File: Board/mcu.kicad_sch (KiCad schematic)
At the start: 5 parts, among them J1 USB_C_Receptacle_USB2.0_14P, U1 NCP1117-3.3_SOT223, U2 RP2040

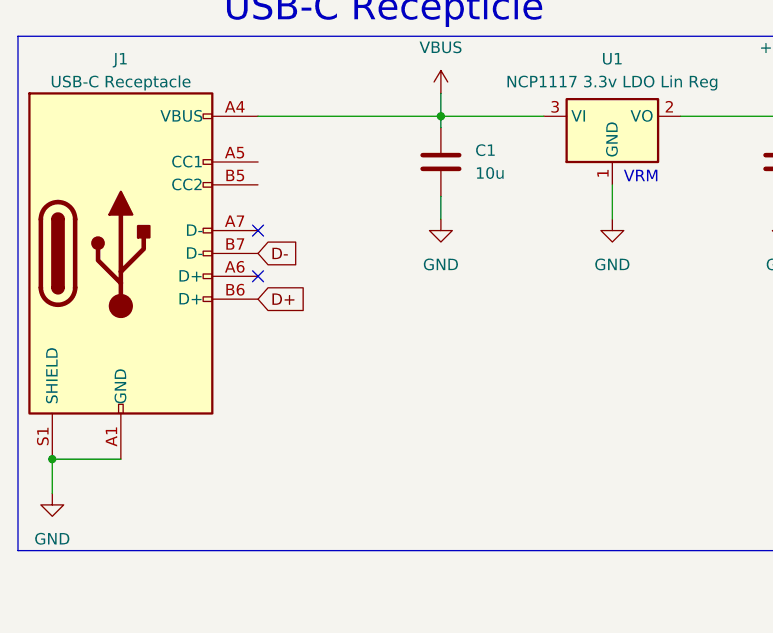
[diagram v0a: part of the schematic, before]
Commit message: Added pulldowns to USBC Receptacle CC1 and CC2 pins
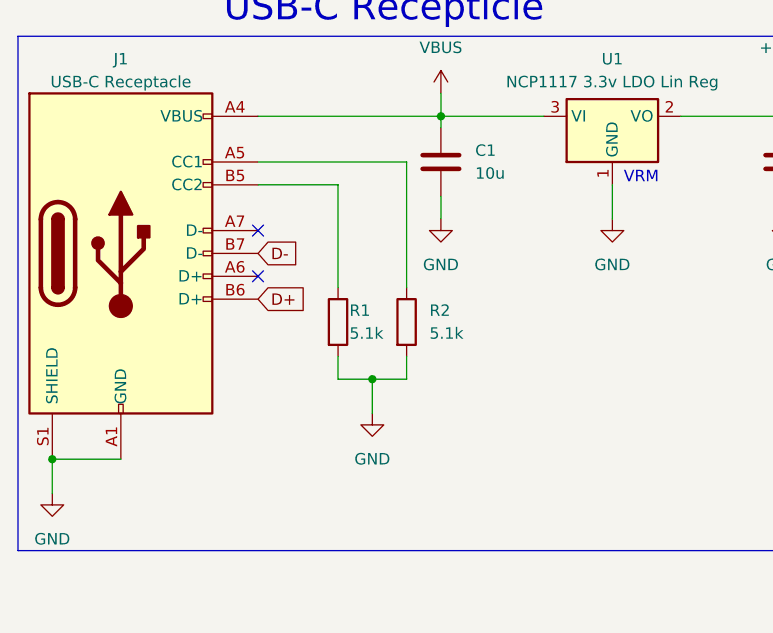
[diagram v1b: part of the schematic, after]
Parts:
- added R1, R2: 5.1k, Resistor_SMD:R_0603_1608Metric, symbol Device:R
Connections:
- net GND: now also R1.2, R2.2
- net at J1.A5 (CC1): now also R2.1
- net at J1.B5 (CC2): now also R1.1
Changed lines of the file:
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@@
   (junction (at 66.04 36.83) (diameter 0) (color 0 0 0 0)
+  )
+  (junction (at 58.42 66.04) (diameter 0) (color 0 0 0 0)
   )
   (junction (at 104.14 36.83) (diameter 0) (color 0 0 0 0)
@@
   (no_connect (at 45.72 49.53))
   (no_connect (at 45.72 54.61))
+  (wire (pts (xy 62.23 66.04) (xy 62.23 63.5))
+    (stroke (width 0) (type default))
+  )
+  (wire (pts (xy 58.42 66.04) (xy 62.23 66.04))
+    (stroke (width 0) (type default))
+  )
   (wire (pts (xy 66.04 48.26) (xy 66.04 45.72))
     (stroke (width 0) (type default))
   )
+  (wire (pts (xy 54.61 63.5) (xy 54.61 66.04))
+    (stroke (width 0) (type default))
+  )
   (wire (pts (xy 22.86 74.93) (xy 30.48 74.93))
     (stroke (width 0) (type default))
@@
     (stroke (width 0) (type default))
   )
+  (wire (pts (xy 45.72 41.91) (xy 62.23 41.91))
+    (stroke (width 0) (type default))
+  )
   (wire (pts (xy 45.72 36.83) (xy 66.04 36.83))
     (stroke (width 0) (type default))
   )
+  (wire (pts (xy 54.61 44.45) (xy 54.61 55.88))
+    (stroke (width 0) (type default))
+  )
   (wire (pts (xy 22.86 74.93) (xy 22.86 78.74))
     (stroke (width 0) (type default))
   )
+  (wire (pts (xy 58.42 66.04) (xy 58.42 69.85))
+    (stroke (width 0) (type default))
+  )
   (wire (pts (xy 104.14 34.29) (xy 104.14 36.83))
     (stroke (width 0) (type default))
@@
     (stroke (width 0) (type default))
   )
+  (wire (pts (xy 62.23 41.91) (xy 62.23 55.88))
+    (stroke (width 0) (type default))
+  )
+  (wire (pts (xy 45.72 44.45) (xy 54.61 44.45))
+    (stroke (width 0) (type default))
+  )
   (wire (pts (xy 104.14 36.83) (xy 104.14 38.1))
+    (stroke (width 0) (type default))
+  )
+  (wire (pts (xy 54.61 66.04) (xy 58.42 66.04))
     (stroke (width 0) (type default))
   )
@@
     (property "Intersheetrefs" "${INTERSHEET_REFS}" (at 51.5476 52.07 0)
       (effects (font (size 1.27 1.27)) (justify left) hide)
+    )
+  )
+  (symbol (lib_id "power:GND") (at 58.42 69.85 0) (unit 1)
+    (in_bom yes) (on_board yes) (dnp no) (fields_autoplaced)
+    (property "Reference" "#PWR07" (at 58.42 76.2 0)
+      (effects (font (size 1.27 1.27)) hide)
+    )
+    (property "Value" "GND" (at 58.42 74.93 0)
+      (effects (font (size 1.27 1.27)))
+    )
+    (property "Footprint" "" (at 58.42 69.85 0)
+      (effects (font (size 1.27 1.27)) hide)
+    )
+    (property "Datasheet" "" (at 58.42 69.85 0)
+      (effects (font (size 1.27 1.27)) hide)
+    )
+    (pin "1")
+    (instances
+      (project "ND68"
+        (path "/f6515d16-f8c0-46c5-adb6-b60d73ae282b/e7d003c3-21c2-4dac-954e-30d7425e12ae"
+          (reference "#PWR07") (unit 1)
+        )
+      )
+    )
+  )
+  (symbol (lib_id "Device:R") (at 54.61 59.69 0) (unit 1)
+    (in_bom yes) (on_board yes) (dnp no)
+    (property "Reference" "R1" (at 55.88 58.42 0)
+      (effects (font (size 1.27 1.27)) (justify left))
+    )
+    (property "Value" "5.1k" (at 55.88 60.96 0)
+      (effects (font (size 1.27 1.27)) (justify left))
+    )
+    (property "Footprint" "Resistor_SMD:R_0603_1608Metric" (at 52.832 59.69 90)
+      (effects (font (size 1.27 1.27)) hide)
+    )
+    (property "Datasheet" "~" (at 54.61 59.69 0)
+      (effects (font (size 1.27 1.27)) hide)
+    )
+    (property "DigiKey" "311-5.10KHRCT-ND" (at 54.61 59.69 0)
+      (effects (font (size 1.27 1.27)) hide)
+    )
+    (pin "2")
+    (pin "1")
+    (instances
+      (project "ND68"
+        (path "/f6515d16-f8c0-46c5-adb6-b60d73ae282b/e7d003c3-21c2-4dac-954e-30d7425e12ae"
+          (reference "R1") (unit 1)
+        )
+      )
     )
   )
@@
         )
       )
+    )
+  )
+  (symbol (lib_id "Device:R") (at 62.23 59.69 0) (unit 1)
+    (in_bom yes) (on_board yes) (dnp no) (fields_autoplaced)
+    (property "Reference" "R2" (at 64.77 58.42 0)
+      (effects (font (size 1.27 1.27)) (justify left))
+    )
+    (property "Value" "5.1k" (at 64.77 60.96 0)
+      (effects (font (size 1.27 1.27)) (justify left))
+    )
+    (property "Footprint" "Resistor_SMD:R_0603_1608Metric" (at 60.452 59.69 90)
+      (effects (font (size 1.27 1.27)) hide)
+    )
+    (property "Datasheet" "~" (at 62.23 59.69 0)
+      (effects (font (size 1.27 1.27)) hide)
+    )
+    (property "DigiKey" "311-5.10KHRCT-ND" (at 62.23 59.69 0)
+      (effects (font (size 1.27 1.27)) hide)
+    )
+    (pin "2")
+    (pin "1")
+    (instances
+      (project "ND68"
+        (path "/f6515d16-f8c0-46c5-adb6-b60d73ae282b/e7d003c3-21c2-4dac-954e-30d7425e12ae"
+          (reference "R2") (unit 1)
+        )
+      )

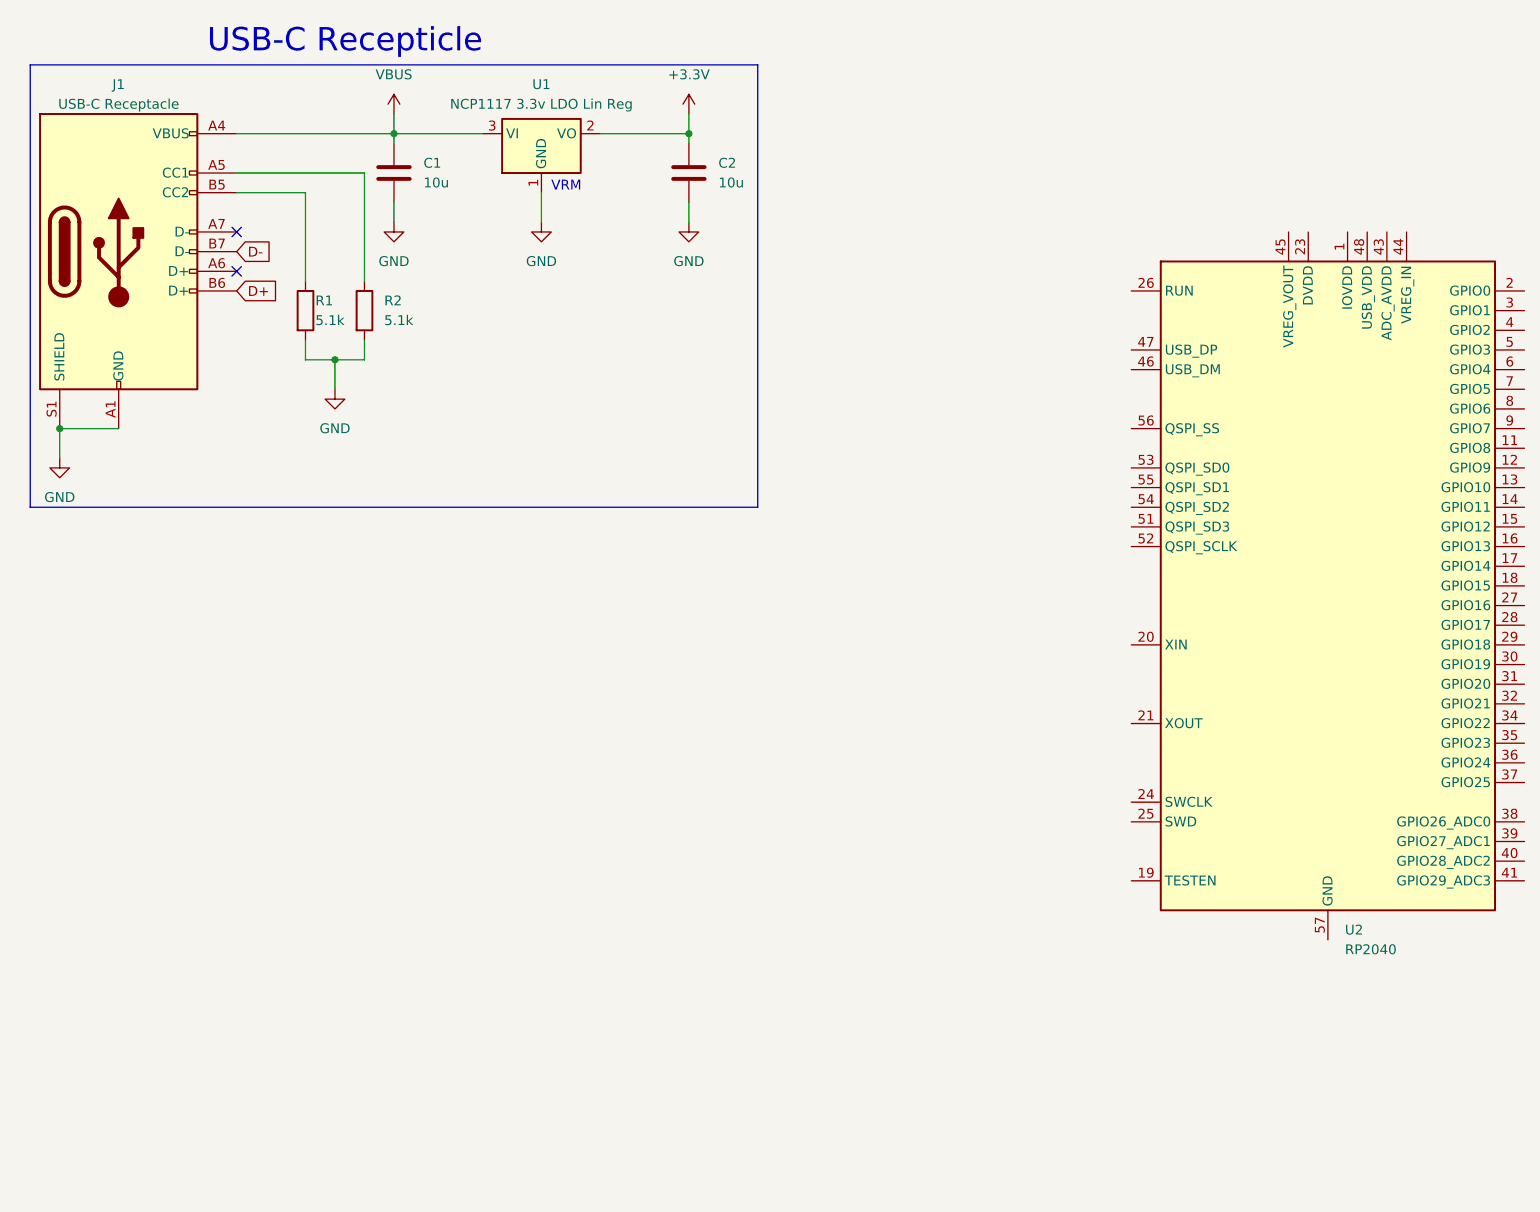
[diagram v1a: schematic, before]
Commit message: Added mcu power pin decoupling capacitors
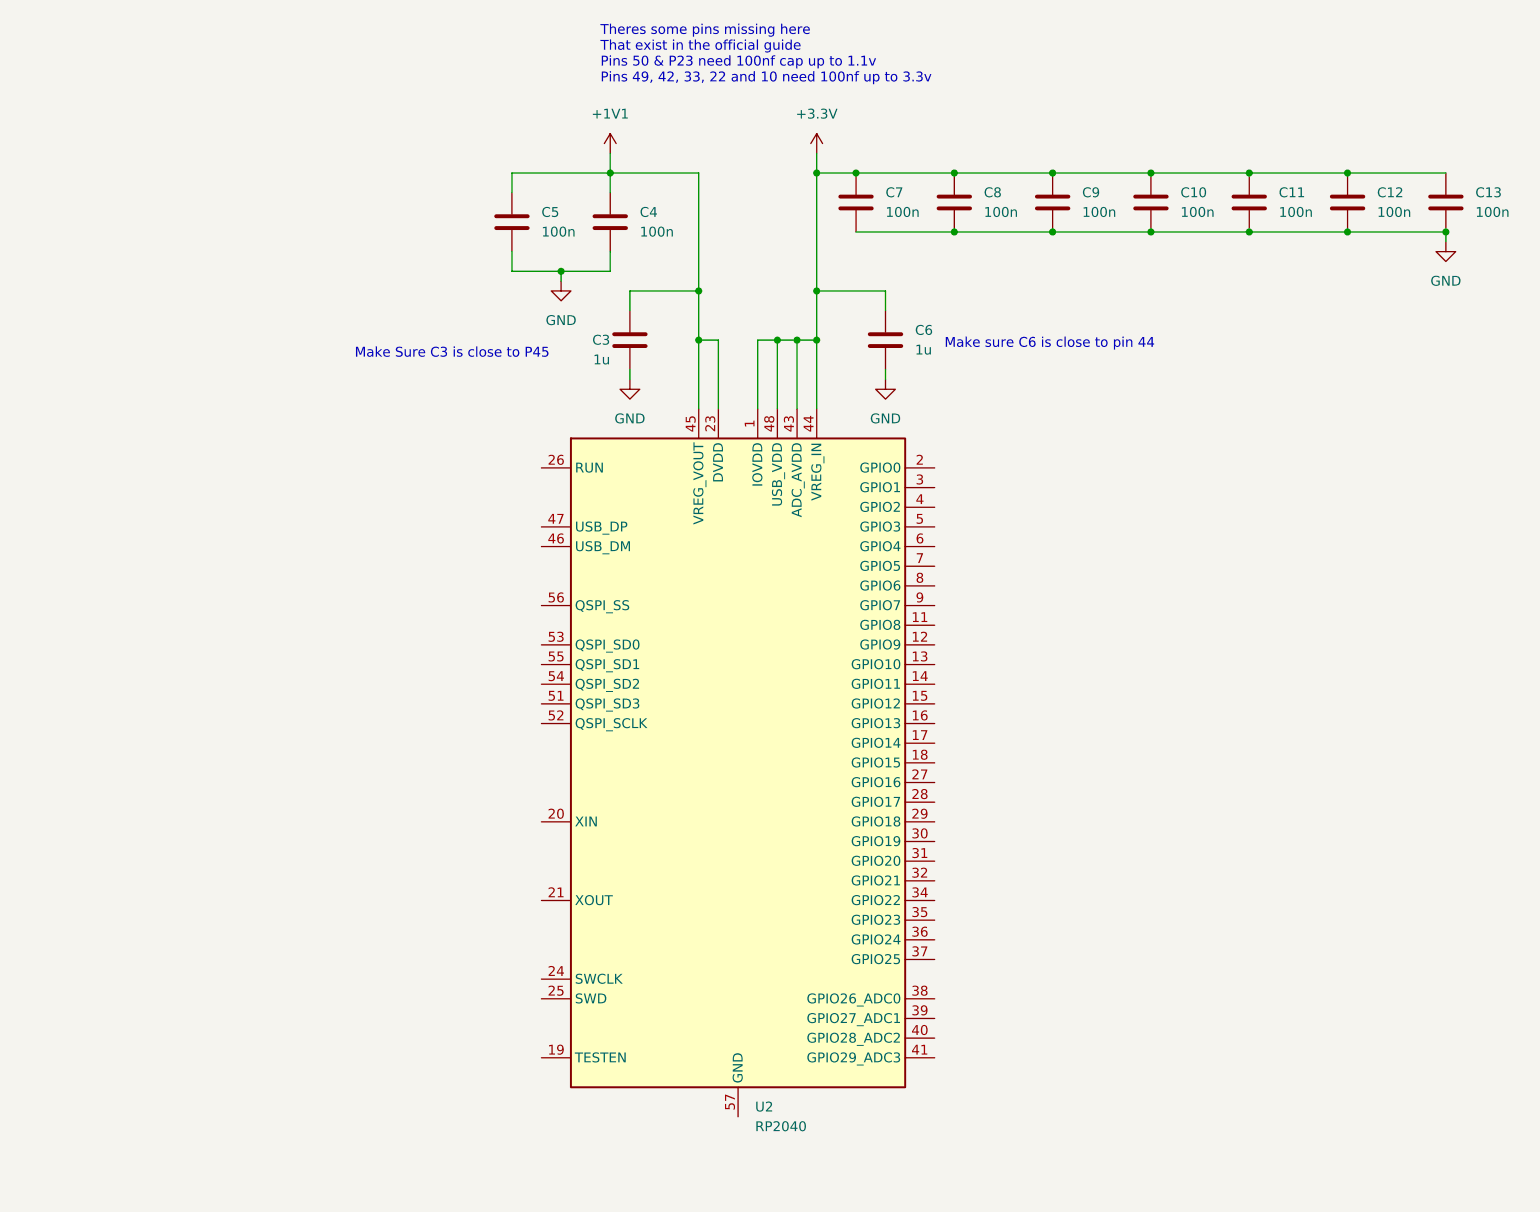
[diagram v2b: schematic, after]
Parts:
- removed C1, C2: 10u, Capacitor_SMD:C_0805_2012Metric, symbol Device:C
- removed J1: USB_C_Receptacle_USB2.0_14P, symbol Connector:USB_C_Receptacle_USB2.0_14P
- removed R1, R2: 5.1k, Resistor_SMD:R_0603_1608Metric, symbol Device:R
- removed U1: NCP1117-3.3_SOT223, Package_TO_SOT_SMD:SOT-223-3_TabPin2, symbol Regulator_Linear:NCP1117-3.3_SOT223
- added C10, C11, C12, C13, C4, C5, C7, C8, C9: 100n, Capacitor_SMD:C_0201_0603Metric, symbol Device:C
- added C3, C6: 1u, Capacitor_SMD:C_0402_1005Metric, symbol Device:C
- U2: footprint RP2040:RP2040-QFN-56 -> Package_DFN_QFN:QFN-56-1EP_7x7mm_P0.4mm_EP3.2x3.2mm
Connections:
- net +3.3V: now also U2.1 (IOVDD), U2.10 (IOVDD), U2.22 (IOVDD), U2.33 (IOVDD), U2.42 (IOVDD), U2.43 (ADC_AVDD), U2.44 (VREG_IN), U2.48 (USB_VDD), U2.49 (IOVDD), C10.1, C11.1, C12.1, C13.1, C6.1, C7.1, C8.1, C9.1
- net GND: now also C10.2, C11.2, C12.2, C13.2, C3.2, C4.2, C5.2, C6.2, C7.2, C8.2, C9.2
- net +1V1: now reaches U2.23 (DVDD), U2.50 (DVDD)
- net +1V1: now also U2.45 (VREG_VOUT), C3.1, C4.1, C5.1
- no-connect marks 2 -> 0
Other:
- note added: "Make Sure C3 is close to P45"
- note added: "Make sure C6 is close to pin 44"
- note added: "Theres some pins missing here That exist in the official guide Pins 50 & P23 need 100nf cap up to 1.1v Pins 49, 42, 33, 22 and 10 need 100nf up to 3.3v"
- note removed: "USB-C Recepticle"
- note removed: "VRM"

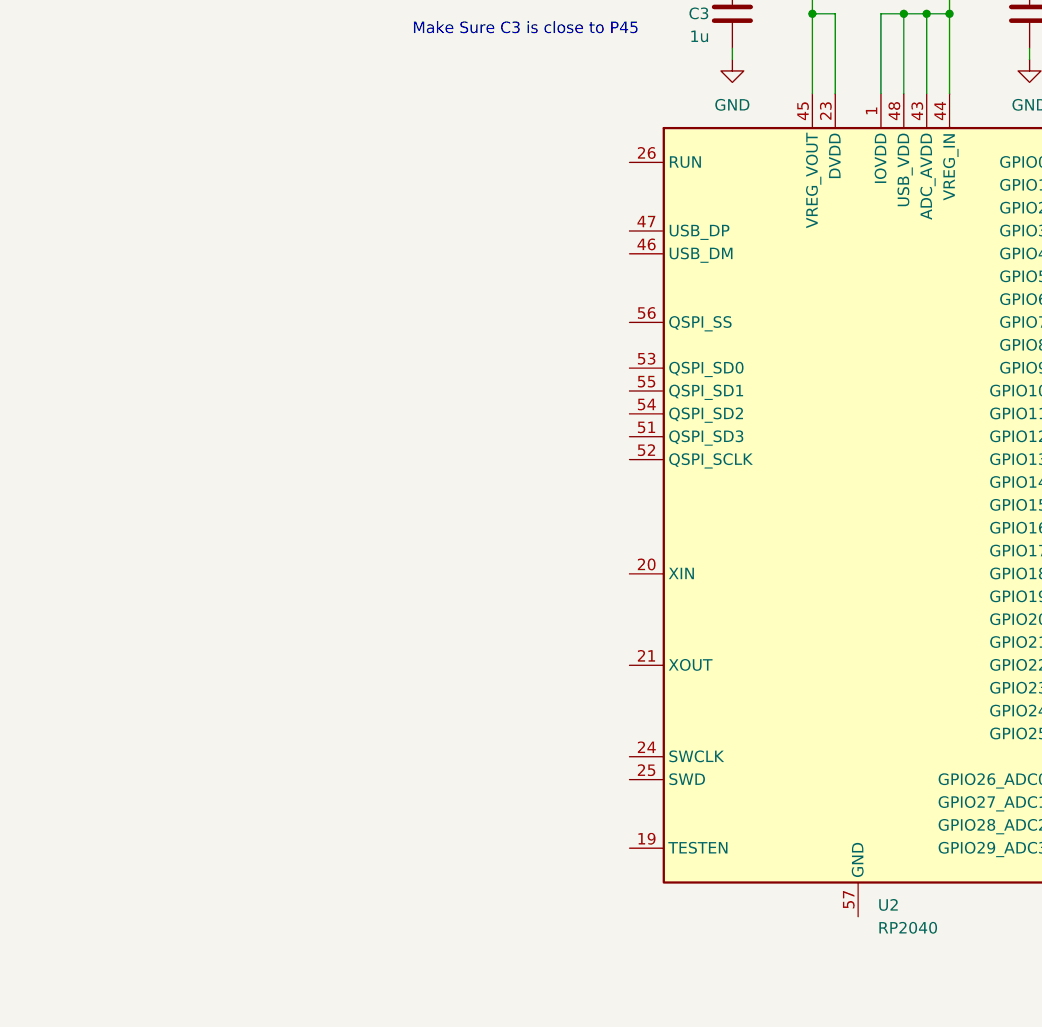
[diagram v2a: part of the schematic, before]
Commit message: Added the rest of the required stuff tp the mcu
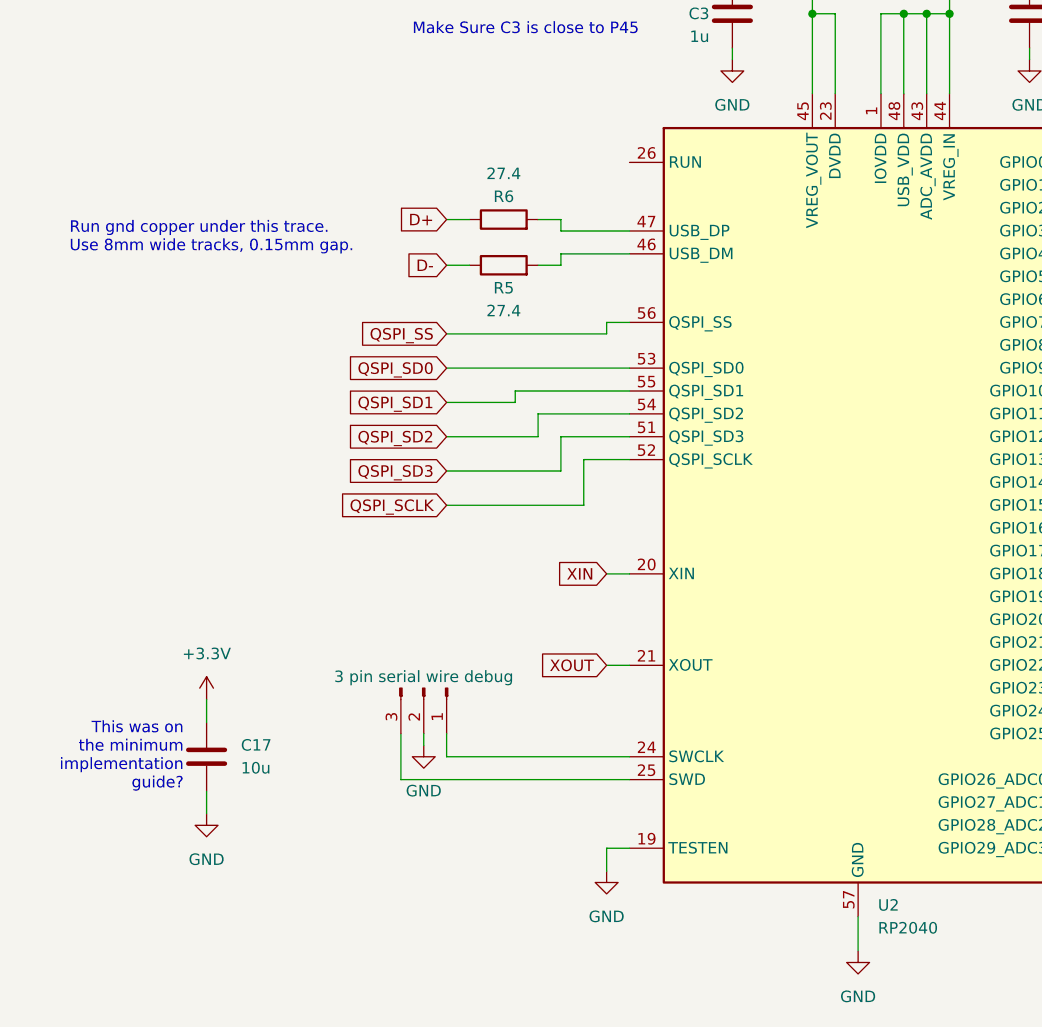
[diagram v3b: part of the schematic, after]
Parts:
- added C17: 10u, Capacitor_SMD:C_0805_2012Metric, symbol Device:C
- added J2: Conn_01x03_Pin, Connector_PinHeader_2.00mm:PinHeader_1x03_P2.00mm_Vertical, symbol Connector:Conn_01x03_Pin
- added R5, R6: 27.4, Resistor_SMD:R_0402_1005Metric, symbol Device:R
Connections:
- net +3.3V: now also C17.1
- net GND: now also U2.19 (TESTEN), U2.57 (GND), C17.2, J2.2 (Pin_2)
- net XIN: now reaches U2.20 (XIN)
- net XOUT: now reaches U2.21 (XOUT)
- net at U2.24 (SWCLK): now also J2.1 (Pin_1)
- net at U2.25 (SWD): now also J2.3 (Pin_3)
- net at U2.46 (USB_DM): now also R5.2
- net at U2.47 (USB_DP): now also R6.2
- net QSPI_SD3: now reaches U2.51 (QSPI_SD3)
- net QSPI_SCLK: now reaches U2.52 (QSPI_SCLK)
- net QSPI_SD0: now reaches U2.53 (QSPI_SD0)
- net QSPI_SD2: now reaches U2.54 (QSPI_SD2)
- net QSPI_SD1: now reaches U2.55 (QSPI_SD1)
- net QSPI_SS: now reaches U2.56 (QSPI_SS)
- new net D+: R6.1
- new net D-: R5.1
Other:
- note added: "Run gnd copper under this trace. Use 8mm wide tracks, 0.15mm gap."
- note added: "This was on the minimum implementation guide?"

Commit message: WIP PCB Layout
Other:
- note added: "Run gnd copper under this trace. Use 8mm wide tracks, 0.15mm gap. Make sure resistors are close to mcu."
- note removed: "Run gnd copper under this trace. Use 8mm wide tracks, 0.15mm gap."
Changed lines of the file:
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@@
     (effects (font (size 1.27 1.27)) (justify left bottom))
   )
-  (text "Run gnd copper under this trace. \nUse 8mm wide tracks, 0.15mm gap."
-    (at 22.86 90.17 0)
+  (text "Run gnd copper under this trace. \nUse 8mm wide tracks, 0.15mm gap.\nMake sure resistors are close to mcu."
+    (at 21.59 90.17 0)
     (effects (font (size 1.27 1.27)) (justify left bottom))
   )

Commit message: VERY BASIC pcb layout
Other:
- note added: "Theres some pins missing here That exist in the official guide Pins 50 & 23 need 100nf cap up to 1.1v Pins 49, 42, 33, 22 and 10 need 100nf up to 3.3v"
- note removed: "Theres some pins missing here That exist in the official guide Pins 50 & P23 need 100nf cap up to 1.1v Pins 49, 42, 33, 22 and 10 need 100nf up to 3.3v"
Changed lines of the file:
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@@
     (effects (font (size 1.27 1.27)) (justify left bottom))
   )
-  (text "Theres some pins missing here\nThat exist in the official guide\nPins 50 & P23 need 100nf cap up to 1.1v\nPins 49, 42, 33, 22 and 10 need 100nf up to 3.3v"
+  (text "Theres some pins missing here\nThat exist in the official guide\nPins 50 & 23 need 100nf cap up to 1.1v\nPins 49, 42, 33, 22 and 10 need 100nf up to 3.3v"
     (at 92.71 30.48 0)
     (effects (font (size 1.27 1.27)) (justify left bottom))
